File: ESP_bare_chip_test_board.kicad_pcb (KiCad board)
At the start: 4 copper layers, 0 parts

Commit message: Copy in component arrangement from SDMMC test design
Already had an efficient arrangement for the SPI flash chip, Clock
crystal, and Antenna.
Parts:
- added C4: 2.2uF, Capacitor_SMD:C_0402_1005Metric, F.Cu at (146.2, 95.4)
- added C5: 0.1uF, Capacitor_SMD:C_0402_1005Metric, F.Cu at (147.4, 79.0)
- added C701: 10pF, Capacitor_SMD:C_0603_1608Metric, F.Cu at (146.8, 73.3)
- added C702: 10pF, Capacitor_SMD:C_0603_1608Metric, F.Cu at (146.8, 66.9)
- added C703: 2.7pF, Capacitor_SMD:C_0402_1005Metric, F.Cu at (143.6, 62.9)
- added C704: 4.7pF, Capacitor_SMD:C_0402_1005Metric, F.Cu at (142.1, 64.0)
- added C707: 1uF, Capacitor_SMD:C_0402_1005Metric, F.Cu at (143.8, 65.9)
- added C709: 1uF, Capacitor_SMD:C_0402_1005Metric, F.Cu at (132.3, 75.8)
- added C710: 10nF, Capacitor_SMD:C_0402_1005Metric, F.Cu at (143.8, 66.9)
- added C712: 0.1uF, Capacitor_SMD:C_0402_1005Metric, F.Cu at (131.8, 78.5)
- added C713: 0.1uF, Capacitor_SMD:C_0402_1005Metric, F.Cu at (132.8, 69.0)
- added C714: 0.1uF, Capacitor_SMD:C_0402_1005Metric, F.Cu at (143.1, 71.8)
- added C715: TBD, Capacitor_SMD:C_0402_1005Metric, F.Cu at (146.6, 64.5)
- added E701: ANTENNA-GROUNDEDTRACE-15.2MM, RF_Antenna_custom:Texas_SWRA117D_2.4GHz_Left, F.Cu at (145.4, 60.6)
- added L701: 1.6nH, Inductor_SMD:L_0402_1005Metric, F.Cu at (141.5, 65.4)
- added L703: TBD, Inductor_SMD:L_0402_1005Metric, F.Cu at (145.2, 63.1)
- added Q701: 40MHz, Crystal:Crystal_SMD_3225-4Pin_3.2x2.5mm, F.Cu at (146.8, 70.1)
- added R1: 22Ω, Resistor_SMD:R_0402_1005Metric, F.Cu at (139.1, 84.7)
- added R10: 50kΩ, Resistor_SMD:R_0402_1005Metric, F.Cu at (143.1, 78.5)
- added R11: 10kΩ, Resistor_SMD:R_0402_1005Metric, F.Cu at (140.5, 90.3)
- added R2: 50kΩ, Resistor_SMD:R_0402_1005Metric, F.Cu at (145.0, 76.5)
- added R3: 50kΩ, Resistor_SMD:R_0402_1005Metric, F.Cu at (140.3, 81.5)
- added R4: 50kΩ, Resistor_SMD:R_0402_1005Metric, F.Cu at (146.8, 76.5)
- added R5: 50kΩ, Resistor_SMD:R_0402_1005Metric, F.Cu at (140.3, 79.5)
- added R6: 50kΩ, Resistor_SMD:R_0402_1005Metric, F.Cu at (141.4, 76.5)
- added R7: 50kΩ, Resistor_SMD:R_0402_1005Metric, F.Cu at (141.4, 78.5)
- added R702: TBD, 24nH to start, Resistor_SMD:R_0402_1005Metric, F.Cu at (144.0, 68.2)
- added R703: 0, Resistor_SMD:R_0402_1005Metric, F.Cu at (133.6, 75.8)
- added R704: 0, Resistor_SMD:R_0402_1005Metric, F.Cu at (134.6, 75.8)
- added R705: 0, Resistor_SMD:R_0402_1005Metric, F.Cu at (135.6, 75.8)
- added R706: 0, Resistor_SMD:R_0402_1005Metric, F.Cu at (136.7, 75.8)
- added R707: 0, Resistor_SMD:R_0402_1005Metric, F.Cu at (137.7, 75.8)
- added R8: 50kΩ, Resistor_SMD:R_0402_1005Metric, F.Cu at (145.0, 78.5)
- added R9: 50kΩ, Resistor_SMD:R_0402_1005Metric, F.Cu at (143.1, 76.5)
- added REF**: U.FL_Molex_MCRF_73412-0110_Vertical, Connector_Coaxial:U.FL_Molex_MCRF_73412-0110_Vertical, F.Cu at (159.4, 55.9)
- added U1: ~, Package_BGA_custom:FBGA-153_11.5x13mm_Layout14x14_P0.5mm_Ball0.3_Pad0.3mm_NSMD, F.Cu at (148.1, 87.1)
- added U701: W25Q128JVS, Package_SO:SOIC-8_5.23x5.23mm_P1.27mm, F.Cu at (135.4, 82.2)
- added U702: ESP32-S3, Package_DFN_QFN:QFN-56-1EP_7x7mm_P0.4mm_EP5.6x5.6mm, F.Cu at (138.0, 69.7)
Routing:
- net (no net): track 0.00 -> 337.9 mm, vias 0 -> 22
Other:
- board outline added: 57.1 x 69.8 mm

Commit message: squash! Copy in component arrangement from SDMMC test design
Using it as a template.
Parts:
- added C201: 100nF/50V, Capacitor_SMD:C_0603_1608Metric, F.Cu at (86.1, 64.9)
- added C202: 1uF/50V, Capacitor_SMD:C_0805_2012Metric, F.Cu at (88.2, 82.4)
- added C203: 4.7uF/25V, Capacitor_SMD:C_0805_2012Metric, F.Cu at (88.2, 85.5)
- added C204: 100nF/50V, Capacitor_SMD:C_0603_1608Metric, F.Cu at (86.1, 67.4)
- added C205: 22uF/6.3V, Capacitor_SMD:C_0603_1608Metric, F.Cu at (86.1, 69.9)
- added C301: 10pF, Capacitor_SMD:C_0603_1608Metric, F.Cu at (127.3, 62.4)
- added C302: 10pF, Capacitor_SMD:C_0603_1608Metric, F.Cu at (127.3, 68.7)
- added C305: 1uF, Capacitor_SMD:C_0402_1005Metric, F.Cu at (106.1, 71.4)
- added C307: 1uF, Capacitor_SMD:C_0402_1005Metric, F.Cu at (106.1, 73.4)
- added C308: 10nF, Capacitor_SMD:C_0402_1005Metric, F.Cu at (106.1, 75.3)
- added C310: 0.1uF, Capacitor_SMD:C_0402_1005Metric, F.Cu at (121.7, 70.8)
- added C311: 0.1uF, Capacitor_SMD:C_0402_1005Metric, F.Cu at (106.1, 79.3)
- added C312: 0.1uF, Capacitor_SMD:C_0402_1005Metric, F.Cu at (106.1, 81.2)
- added C401: 4.7pF, Capacitor_SMD:C_0402_1005Metric, F.Cu at (63.8, 99.4)
- added C402: 2.7pF, Capacitor_SMD:C_0402_1005Metric, F.Cu at (63.8, 101.4)
- added C403: TBD, Capacitor_SMD:C_0402_1005Metric, F.Cu at (63.8, 103.4)
- added C505: 1uF/50V, Capacitor_SMD:C_0805_2012Metric, F.Cu at (99.4, 95.7)
- added D201: B5819W, Diode_SMD:D_SOD-123, F.Cu at (65.3, 87.5)
- added D202: GREEN, LED_SMD:LED_0603_1608Metric, F.Cu at (70.2, 87.2)
- added E401: ANTENNA-GROUNDEDTRACE-15.2MM, RF_Antenna_custom:Texas_SWRA117D_2.4GHz_Left, F.Cu at (75.2, 97.5)
- added J201: Conn_01x06, Connector_PinSocket_2.54mm:PinSocket_1x06_P2.54mm_Vertical, F.Cu at (81.8, 66.0)
- added J501: USB_C_Receptacle, Connector_USB:USB_C_Receptacle_GCT_USB4115-03-C, F.Cu at (97.9, 90.4)
- added L401: 1.6nH, Inductor_SMD:L_0402_1005Metric, F.Cu at (71.8, 99.4)
- added L402: TBD, Inductor_SMD:L_0402_1005Metric, F.Cu at (71.8, 101.4)
- added Q301: 40MHz, Crystal:Crystal_SMD_3225-4Pin_3.2x2.5mm, F.Cu at (127.3, 65.5)
- added R201: 10kΩ, Resistor_SMD:R_0603_1608Metric, F.Cu at (86.1, 72.4)
- added R202: 10kΩ, Resistor_SMD:R_0603_1608Metric, F.Cu at (86.1, 74.9)
- added R301: TBD, 24nH to start, Resistor_SMD:R_0402_1005Metric, F.Cu at (124.5, 63.6)
- added R302: 0, Resistor_SMD:R_0402_1005Metric, F.Cu at (114.9, 70.3)
- added R303: 0, Resistor_SMD:R_0402_1005Metric, F.Cu at (115.9, 70.3)
- added R304: 0, Resistor_SMD:R_0402_1005Metric, F.Cu at (116.9, 70.3)
- added R305: 0, Resistor_SMD:R_0402_1005Metric, F.Cu at (117.9, 70.3)
- added R306: 0, Resistor_SMD:R_0402_1005Metric, F.Cu at (118.9, 70.3)
- added SW201: SW_Push, Button_Switch_SMD_custom:SW_PUSHBUTTON_2PIN_SMD_3×4×2.0, F.Cu at (82.7, 83.0)
- added SW202: SW_Push, Button_Switch_SMD_custom:SW_PUSHBUTTON_2PIN_SMD_3×4×2.0, F.Cu at (82.7, 87.2)
- added U201: TLV75533PDBV, Package_TO_SOT_SMD:SOT-23-5, F.Cu at (86.7, 78.4)
- added U202: ESP32-S3-MINI-1, Espressif:ESP32-S3-MINI-1, F.Cu at (70.9, 77.3)
- added U301: W25Q128JVS, Package_SO:SOIC-8_5.23x5.23mm_P1.27mm, F.Cu at (118.6, 74.2)
- added U302: ESP32-S3, Package_DFN_QFN:QFN-56-1EP_7x7mm_P0.4mm_EP5.6x5.6mm, F.Cu at (118.4, 65.1)
- added U401: MASWSS0179, Package_TO_SOT_SMD:SOT-23-6, F.Cu at (67.8, 100.7)
- added U501: DT1240A-04LP-7, Package_DFN_QFN:Diodes_UDFN-10_1.0x2.5mm_P0.5mm, F.Cu at (103.1, 96.2)
- added U502: FUSB302BMPX, Package_DFN_QFN:WQFN-14-1EP_2.5x2.5mm_P0.5mm_EP1.45x1.45mm, F.Cu at (94.8, 96.5)
- moved R10 1.09 mm to (143.8, 77.6)
- moved R8 1.09 mm to (145.7, 77.6)
- moved C715 1.09 mm to (147.2, 63.6)
- moved E701 1.09 mm to (146.1, 59.7)
- moved C4 1.09 mm to (146.8, 94.5)
- moved C709 1.09 mm to (132.9, 74.9)
- moved C712 1.09 mm to (132.5, 77.6)
- moved C714 1.09 mm to (143.8, 70.9)
- moved R11 1.09 mm to (141.1, 89.4)
- moved R2 1.09 mm to (145.7, 75.6)
- moved R706 1.09 mm to (137.3, 74.9)
- moved R9 1.09 mm to (143.8, 75.6)
- moved U1 1.09 mm to (148.7, 86.2)
- moved U702 1.09 mm to (138.6, 68.8)
- moved R1 1.09 mm to (139.7, 83.8)
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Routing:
- net (no net): track 337.9 -> 87.9 mm, vias 22 -> 19
- net /ESP32-S3/IO17: track 0.00 -> 24.1 mm
- net /ESP32-S3/IO42: track 0.00 -> 21.6 mm
- net /USB_D-: track 0.00 -> 21.5 mm
- net Net-(U302-XTAL_N): track 0.00 -> 19.9 mm, vias 0 -> 1
- net /ESP32-S3/IO41: track 0.00 -> 18.0 mm
- net /USB_D+: track 0.00 -> 17.7 mm
- net /ESP32-S3/ESP32-S3-core/SPID: track 0.00 -> 16.5 mm
- net /ESP32-S3/IO13: track 0.00 -> 16.4 mm
- net /ESP32-S3/ESP32-S3-core/VDD_SPI: track 0.00 -> 15.8 mm, vias 0 -> 1
- net /ESP32-S3/IO39: track 0.00 -> 15.0 mm
- net /ESP32-S3/IO40: track 0.00 -> 14.9 mm
- net /ESP32-S3/IO26: track 0.00 -> 13.4 mm
- net /ESP32-S3/IO21: track 0.00 -> 13.4 mm
- net /ESP32-S3/IO18: track 0.00 -> 11.1 mm
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
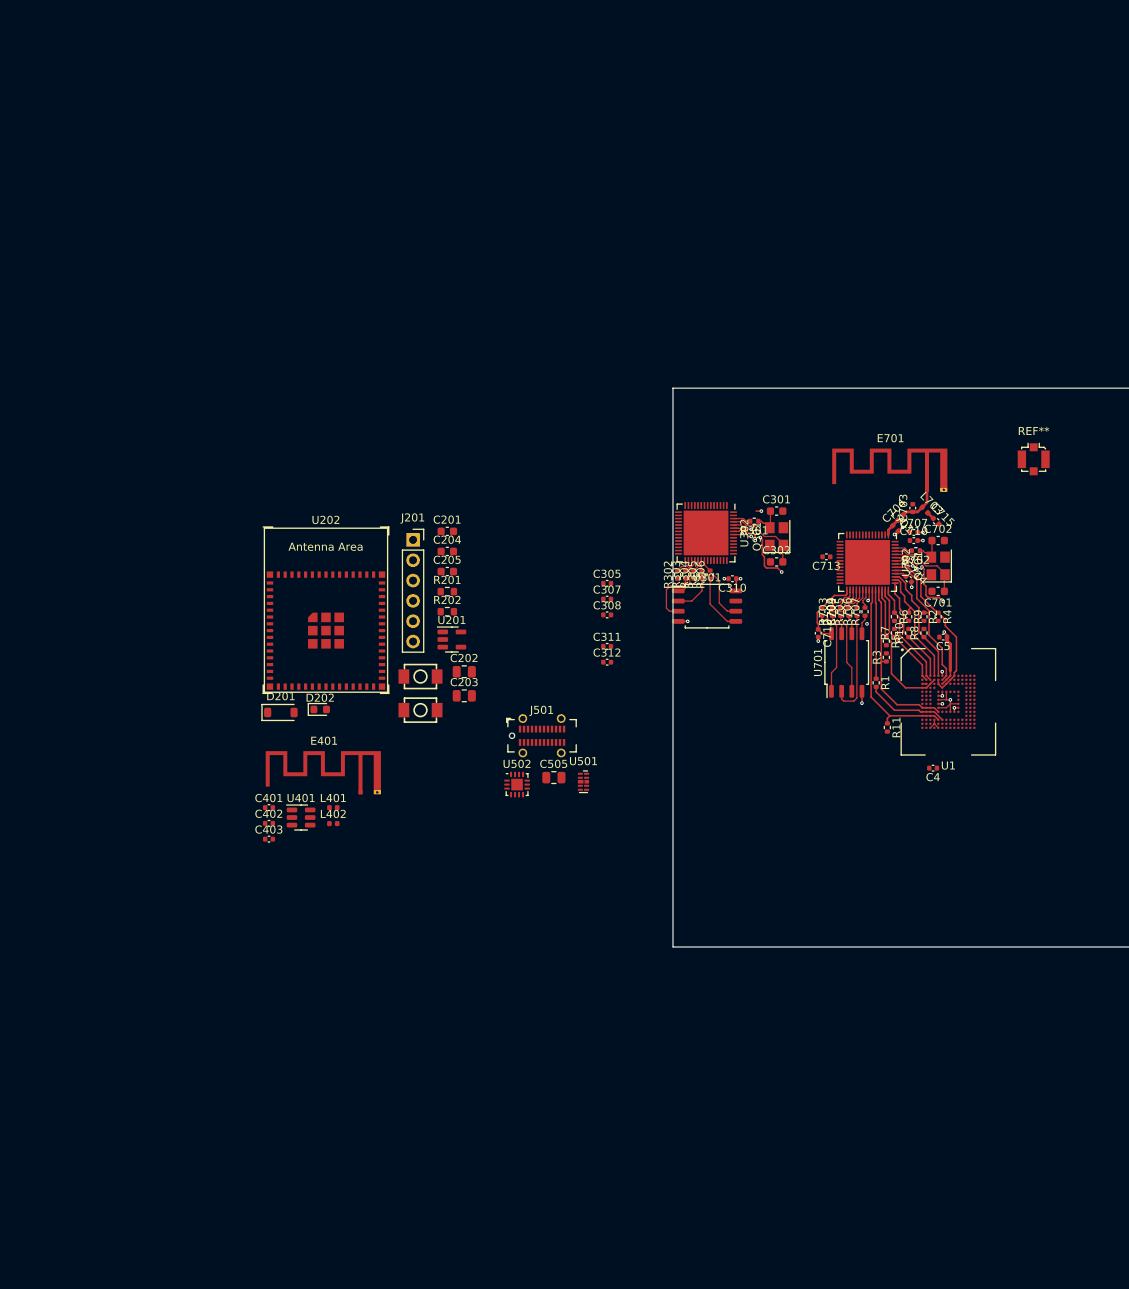
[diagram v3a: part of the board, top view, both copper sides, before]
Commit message: PCB changes, added useful connectors
Added a whole bunch of things that should make it useful - e.g.
ethernet, an extra flash chip for general storage, piicodev connectors
for I2C.

Also added a GPIB connector footprint; dev-board version worked nicely,
but may as well make this work for that too. Saves bying dev boards : )
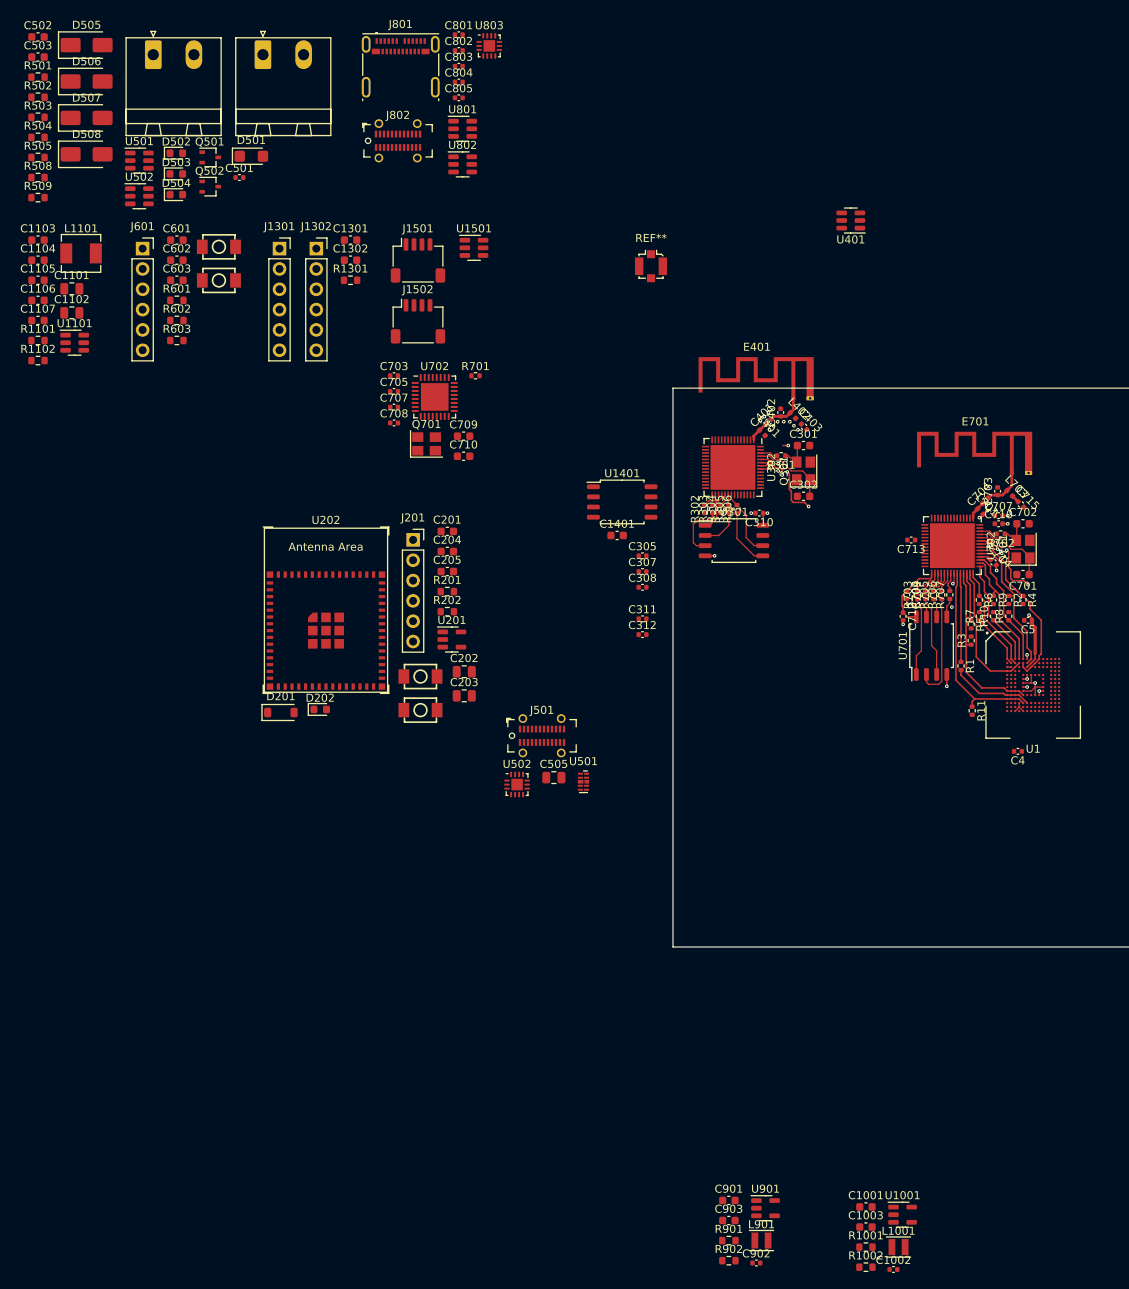
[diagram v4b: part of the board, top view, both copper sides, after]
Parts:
- added C1001: 10uF/10V, Capacitor_SMD:C_0603_1608Metric, F.Cu at (138.4, 149.3)
- added C1002: 22pF, Capacitor_SMD:C_0402_1005Metric, F.Cu at (141.9, 157.2)
- added C1003: 22uF/6.3V, Capacitor_SMD:C_0603_1608Metric, F.Cu at (138.4, 151.8)
- added C1101: 10uF/25v, Capacitor_SMD:C_0805_2012Metric, F.Cu at (39.2, 34.6)
- added C1102: 10uF/25v, Capacitor_SMD:C_0805_2012Metric, F.Cu at (39.2, 37.6)
- added C1103: 100nF, Capacitor_SMD:C_0603_1608Metric, F.Cu at (34.9, 28.5)
- added C1104: 10uF/10V, Capacitor_SMD:C_0603_1608Metric, F.Cu at (34.9, 31.0)
- added C1105: 10uF/10V, Capacitor_SMD:C_0603_1608Metric, F.Cu at (34.9, 33.5)
- added C1106: 10uF/10V, Capacitor_SMD:C_0603_1608Metric, F.Cu at (34.9, 36.0)
- added C1107: 10uF/10V, Capacitor_SMD:C_0603_1608Metric, F.Cu at (34.9, 38.5)
- added C1301: 22uF/6.3V, Capacitor_SMD:C_0603_1608Metric, F.Cu at (74.0, 28.5)
- added C1302: 22uF/6.3V, Capacitor_SMD:C_0603_1608Metric, F.Cu at (74.0, 31.0)
- added C1401: 100nF/50V, Capacitor_SMD:C_0603_1608Metric, F.Cu at (107.3, 65.4)
- added C501: 1uF/25V, Capacitor_SMD:C_0402_1005Metric, F.Cu at (60.1, 20.7)
- added C502: 100nF/50V, Capacitor_SMD:C_0603_1608Metric, F.Cu at (34.9, 3.09)
- added C503: 100nF/50V, Capacitor_SMD:C_0603_1608Metric, F.Cu at (34.9, 5.60)
- added C601: 100nF/50V, Capacitor_SMD:C_0603_1608Metric, F.Cu at (52.3, 28.5)
- added C602: 100nF/50V, Capacitor_SMD:C_0603_1608Metric, F.Cu at (52.3, 31.0)
- added C603: 22uF/6.3V, Capacitor_SMD:C_0603_1608Metric, F.Cu at (52.3, 33.5)
- added C703: 1uF, Capacitor_SMD:C_0402_1005Metric, F.Cu at (79.4, 45.4)
- added C705: 10nF, Capacitor_SMD:C_0402_1005Metric, F.Cu at (79.4, 47.4)
- added C707: 0.1uF, Capacitor_SMD:C_0402_1005Metric, F.Cu at (79.4, 49.4)
- added C708: 0.1uF, Capacitor_SMD:C_0402_1005Metric, F.Cu at (79.4, 51.3)
- added C709: 10pF, Capacitor_SMD:C_0603_1608Metric, F.Cu at (88.1, 53.0)
- added C710: 10pF, Capacitor_SMD:C_0603_1608Metric, F.Cu at (88.1, 55.5)
- added C801: 220pF, Capacitor_SMD:C_0402_1005Metric, F.Cu at (87.5, 2.82)
- added C802: 100nF/50V, Capacitor_SMD:C_0402_1005Metric, F.Cu at (87.5, 4.79)
- added C803: 220pF, Capacitor_SMD:C_0402_1005Metric, F.Cu at (87.5, 6.76)
- added C804: 100nF/50V, Capacitor_SMD:C_0402_1005Metric, F.Cu at (87.5, 8.73)
- added C805: 1uF/25V, Capacitor_SMD:C_0402_1005Metric, F.Cu at (87.5, 10.7)
- added C901: 10uF/10V, Capacitor_SMD:C_0603_1608Metric, F.Cu at (121.3, 148.5)
- added C902: 22pF, Capacitor_SMD:C_0402_1005Metric, F.Cu at (124.7, 156.3)
- added C903: 22uF/6.3V, Capacitor_SMD:C_0603_1608Metric, F.Cu at (121.3, 151.0)
- added D501: SMF5V0A, Diode_SMD:D_SMF, F.Cu at (61.6, 18.0)
- added D502: YELLOW, LED_SMD:LED_0603_1608Metric, F.Cu at (52.2, 17.6)
- added D503: GREEN, LED_SMD:LED_0603_1608Metric, F.Cu at (52.2, 20.2)
- added D504: GREEN, LED_SMD:LED_0603_1608Metric, F.Cu at (52.2, 22.8)
- added D505: SS210, Diode_SMD:D_SMA, F.Cu at (41.0, 4.11)
- added D506: SS210, Diode_SMD:D_SMA, F.Cu at (41.0, 8.66)
- added D507: SS210, Diode_SMD:D_SMA, F.Cu at (41.0, 13.2)
- added D508: SS210, Diode_SMD:D_SMA, F.Cu at (41.0, 17.8)
- added J1301: Conn_01x06, Connector_PinSocket_2.54mm:PinSocket_1x06_P2.54mm_Vertical, F.Cu at (65.1, 29.5)
- added J1302: Conn_01x06, Connector_PinSocket_2.54mm:PinSocket_1x06_P2.54mm_Vertical, F.Cu at (69.7, 29.5)
- added J1501: Conn_01x04, Connector_JST:JST_SH_SM04B-SRSS-TB_1x04-1MP_P1.00mm_Horizontal, F.Cu at (82.4, 31.0)
- added J1502: Conn_01x04, Connector_JST:JST_SH_SM04B-SRSS-TB_1x04-1MP_P1.00mm_Horizontal, F.Cu at (82.4, 38.6)
- added J501: DAISY_CHAIN, Connector_TerminalBlock_custom:Ningbo_Xinlaiya_XY2500R-D-5.08-2P_1x02_P5.08mm_Horizontal, F.Cu at (49.3, 5.30)
- added J502: PWR_IN, Connector_TerminalBlock_custom:Ningbo_Xinlaiya_XY2500R-D-5.08-2P_1x02_P5.08mm_Horizontal, F.Cu at (63.0, 5.30)
- added J601: Conn_01x06, Connector_PinSocket_2.54mm:PinSocket_1x06_P2.54mm_Vertical, F.Cu at (48.0, 29.5)
- added J801: USB_C_Receptacle, Connector_USB:USB_C_Receptacle_Molex_105450-0101, F.Cu at (80.3, 6.82)
- added J802: USB_C_Receptacle, Connector_USB:USB_C_Receptacle_GCT_USB4115-03-C, F.Cu at (79.9, 16.1)
- added L1001: 2.2uH, Inductor_SMD:L_Changjiang_FNR252012S, F.Cu at (142.5, 154.4)
- added L1101: 3.3uH/1.2mΩ, Inductor_SMD:L_Sunlord_MWSA0402S, F.Cu at (40.3, 30.1)
- added L901: 2.2uH, Inductor_SMD:L_Changjiang_FNR252012S, F.Cu at (125.4, 153.5)
- added Q501: DTC114E, Package_TO_SOT_SMD:SOT-323_SC-70, F.Cu at (56.4, 18.1)
- added Q502: DTC114E, Package_TO_SOT_SMD:SOT-323_SC-70, F.Cu at (56.4, 21.8)
- added Q701: 40MHz, Crystal:Crystal_SMD_3225-4Pin_3.2x2.5mm, F.Cu at (83.5, 54.0)
- added R1001: 150kΩ, Resistor_SMD:R_0603_1608Metric, F.Cu at (138.4, 154.4)
- added R1002: 33kΩ, Resistor_SMD:R_0603_1608Metric, F.Cu at (138.4, 156.9)
- added R1101: 56kΩ/1%, Resistor_SMD:R_0603_1608Metric, F.Cu at (34.9, 41.0)
- added R1102: 10kΩ/1%, Resistor_SMD:R_0603_1608Metric, F.Cu at (34.9, 43.5)
- added R1301: 1.5k, Resistor_SMD:R_0603_1608Metric, F.Cu at (74.0, 33.5)
- added R501: 15kΩ/1%, Resistor_SMD:R_0603_1608Metric, F.Cu at (34.9, 8.11)
- added R502: 100kΩ, Resistor_SMD:R_0603_1608Metric, F.Cu at (34.9, 10.6)
- added R503: 10kΩ, Resistor_SMD:R_0603_1608Metric, F.Cu at (34.9, 13.1)
- added R504: 15kΩ/1%, Resistor_SMD:R_0603_1608Metric, F.Cu at (34.9, 15.6)
- added R505: 15kΩ, Resistor_SMD:R_0603_1608Metric, F.Cu at (34.9, 18.1)
- added R508: 100kΩ, Resistor_SMD:R_0603_1608Metric, F.Cu at (34.9, 20.7)
- added R509: 33kΩ, Resistor_SMD:R_0603_1608Metric, F.Cu at (34.9, 23.2)
- added R601: 10kΩ, Resistor_SMD:R_0603_1608Metric, F.Cu at (52.3, 36.0)
- added R602: 100kΩ, Resistor_SMD:R_0603_1608Metric, F.Cu at (52.3, 38.5)
- added R603: 100kΩ, Resistor_SMD:R_0603_1608Metric, F.Cu at (52.3, 41.0)
- added R701: TBD, 24nH to start, Resistor_SMD:R_0402_1005Metric, F.Cu at (89.6, 45.4)
- added R901: 150kΩ, Resistor_SMD:R_0603_1608Metric, F.Cu at (121.3, 153.5)
- added R902: 33kΩ, Resistor_SMD:R_0603_1608Metric, F.Cu at (121.3, 156.1)
- added SW601: SW_Push, Button_Switch_SMD_custom:SW_PUSHBUTTON_2PIN_SMD_3×4×2.0, F.Cu at (57.5, 29.3)
- added SW602: SW_Push, Button_Switch_SMD_custom:SW_PUSHBUTTON_2PIN_SMD_3×4×2.0, F.Cu at (57.5, 33.5)
- added U1001: TLV62569DBV, Package_TO_SOT_SMD:SOT-23-5, F.Cu at (143.0, 150.3)
- added U1101: TPS563201, Package_TO_SOT_SMD:SOT-23-6, F.Cu at (39.5, 41.3)
- added U1401: W25Q128JVS, Package_SO:SOIC-8_5.23x5.23mm_P1.27mm, F.Cu at (108.0, 61.2)
- added U1501: D1213A-04TS-7, Package_TO_SOT_SMD:TSOT-23-6, F.Cu at (89.4, 29.4)
- added U501: TPS2552DBV, Package_TO_SOT_SMD:SOT-23-6, F.Cu at (47.6, 18.5)
- added U502: TPS2552DBV, Package_TO_SOT_SMD:SOT-23-6, F.Cu at (47.6, 23.0)
- added U702: ESP32-C3, Package_DFN_QFN:QFN-32-1EP_5x5mm_P0.5mm_EP3.45x3.45mm, F.Cu at (84.5, 48.1)
- added U801: D1213A-04TS-7, Package_TO_SOT_SMD:TSOT-23-6, F.Cu at (88.0, 14.6)
- added U802: D1213A-04TS-7, Package_TO_SOT_SMD:TSOT-23-6, F.Cu at (88.0, 19.0)
- added U803: FUSB302BPX, Package_DFN_QFN:WQFN-14-1EP_2.5x2.5mm_P0.5mm_EP1.45x1.45mm, F.Cu at (91.3, 4.21)
- added U901: TLV62569DBV, Package_TO_SOT_SMD:SOT-23-5, F.Cu at (125.9, 149.5)
- moved U401 101.4 mm to (136.5, 26.0), turned to 180 degrees
- moved C403 84.4 mm to (130.7, 51.8), turned to -45 degrees
- moved C402 82.0 mm to (127.8, 50.0), turned to 90 degrees
- moved C401 78.9 mm to (126.2, 51.2), turned to 45 degrees
- moved L402 76.8 mm to (129.3, 50.4), turned to -45 degrees
- moved E401 73.2 mm to (129.3, 48.3)
- moved L401 71.2 mm to (125.5, 52.6), turned to -45 degrees
- moved REF** 53.6 mm to (111.6, 31.8)
- moved C5 10.8 mm to (158.7, 76.0)
- moved C702 10.8 mm to (158.1, 63.9)
- moved C710 10.8 mm to (155.0, 63.9)
- moved C713 10.8 mm to (144.1, 66.0)
- moved L701 10.8 mm to (152.7, 62.4)
- moved Q701 10.8 mm to (158.1, 67.1)
- moved R702 10.8 mm to (155.3, 65.2)
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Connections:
- net /ESP32-S3/UART0_Rx renamed /ESP32-C3/UART0_Tx
- net /ESP32-S3/UART0_Tx renamed /ESP32-C3/UART0_Rx
- U302 pad 14: /ESP32-S3/IO9 -> /~{FRAM_CS}
- U302 pad 15: /ESP32-S3/IO10 -> /~{ETH_CS0}
- U302 pad 16: /ESP32-S3/IO11 -> /MOSI
- U302 pad 17: /ESP32-S3/IO12 -> /CLK
- U302 pad 18: /ESP32-S3/IO13 -> /MISO
- U302 pad 52: /ESP32-S3/IO46 -> /ETH_RST
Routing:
- net (no net): track 87.9 -> 117.8 mm, vias 19 -> 32
- net /ESP32-S3/IO13: track 16.4 -> 0.00 mm
- net /ESP32-S3/IO46: track 4.88 -> 0.00 mm, vias 2 -> 0
- net /ESP32-S3/ESP32-S3-core/antenna_experimental/50Ω ANT: track 0.00 -> 4.67 mm
- net /ESP32-S3/IO11: track 3.78 -> 0.00 mm
- net /ESP32-S3/IO12: track 3.30 -> 0.00 mm
- net /ESP32-C3/UART0_Tx: track 5.74 -> 2.87 mm, vias 2 -> 1
- net /ESP32-S3/ESP32-S3-core/RF: track 2.33 -> 4.92 mm
- net /ETH_RST: track 0.00 -> 2.44 mm, vias 0 -> 1
- net /ESP32-C3/UART0_Rx: track 2.26 -> 1.13 mm, vias 2 -> 1
